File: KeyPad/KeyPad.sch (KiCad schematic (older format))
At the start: 9 parts, among them P1 CONN_01X03, SW1 SW_Push_Dual, SW2 SW_Push_Dual, SW3 SW_Push_Dual, SW4 SW_Push_Dual

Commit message: Pcb enrrutada y esquinas redondeadas
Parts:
- P1: footprint (none) -> Connectors_JST:JST_PH_S3B-PH-K_03x2.00mm_Angled
- R1, R2, R3, R4: footprint (none) -> Resistors_SMD:R_0805
- SW1, SW2, SW3, SW4: footprint (none) -> Buttons_Switches_THT:SW_PUSH-12mm
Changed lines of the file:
@@
 F 0 "SW1" H 5700 2800 50  0000 L CNN
 F 1 "SW_Push_Dual" H 5650 2430 50  0000 C CNN
-F 2 "" H 5650 2900 50  0001 C CNN
+F 2 "Buttons_Switches_THT:SW_PUSH-12mm" H 5650 2900 50  0001 C CNN
 F 3 "" H 5650 2900 50  0001 C CNN
 	1    5650 2700
@@
 F 0 "SW2" H 5700 3400 50  0000 L CNN
 F 1 "SW_Push_Dual" H 5650 3030 50  0000 C CNN
-F 2 "" H 5650 3500 50  0001 C CNN
+F 2 "Buttons_Switches_THT:SW_PUSH-12mm" H 5650 3500 50  0001 C CNN
 F 3 "" H 5650 3500 50  0001 C CNN
 	1    5650 3300
@@
 F 0 "SW3" H 5700 4050 50  0000 L CNN
 F 1 "SW_Push_Dual" H 5650 3680 50  0000 C CNN
-F 2 "" H 5650 4150 50  0001 C CNN
+F 2 "Buttons_Switches_THT:SW_PUSH-12mm" H 5650 4150 50  0001 C CNN
 F 3 "" H 5650 4150 50  0001 C CNN
 	1    5650 3950
@@
 F 0 "SW4" H 5700 4650 50  0000 L CNN
 F 1 "SW_Push_Dual" H 5650 4280 50  0000 C CNN
-F 2 "" H 5650 4750 50  0001 C CNN
+F 2 "Buttons_Switches_THT:SW_PUSH-12mm" H 5650 4750 50  0001 C CNN
 F 3 "" H 5650 4750 50  0001 C CNN
 	1    5650 4550
@@
 F 0 "R2" V 5280 3100 50  0000 C CNN
 F 1 "330R" V 5200 3100 50  0000 C CNN
-F 2 "" V 5130 3100 50  0001 C CNN
+F 2 "Resistors_SMD:R_0805" V 5130 3100 50  0001 C CNN
 F 3 "" H 5200 3100 50  0001 C CNN
 	1    5200 3100
@@
 F 0 "P1" H 4250 3100 50  0000 C CNN
 F 1 "CONN_01X03" V 4350 2900 50  0000 C CNN
-F 2 "" H 4250 2900 50  0001 C CNN
+F 2 "Connectors_JST:JST_PH_S3B-PH-K_03x2.00mm_Angled" H 4250 2900 50  0001 C CNN
 F 3 "" H 4250 2900 50  0001 C CNN
 	1    4250 2900
@@
 F 0 "R3" V 5280 3750 50  0000 C CNN
 F 1 "620R" V 5200 3750 50  0000 C CNN
-F 2 "" V 5130 3750 50  0001 C CNN
+F 2 "Resistors_SMD:R_0805" V 5130 3750 50  0001 C CNN
 F 3 "" H 5200 3750 50  0001 C CNN
 	1    5200 3750
@@
 F 0 "R4" V 5280 4350 50  0000 C CNN
 F 1 "1K" V 5200 4350 50  0000 C CNN
-F 2 "" V 5130 4350 50  0001 C CNN
+F 2 "Resistors_SMD:R_0805" V 5130 4350 50  0001 C CNN
 F 3 "" H 5200 4350 50  0001 C CNN
 	1    5200 4350
@@
 F 0 "R1" V 5280 2450 50  0000 C CNN
 F 1 "2K" V 5200 2450 50  0000 C CNN
-F 2 "" V 5130 2450 50  0001 C CNN
+F 2 "Resistors_SMD:R_0805" V 5130 2450 50  0001 C CNN
 F 3 "" H 5200 2450 50  0001 C CNN
 	1    5200 2450

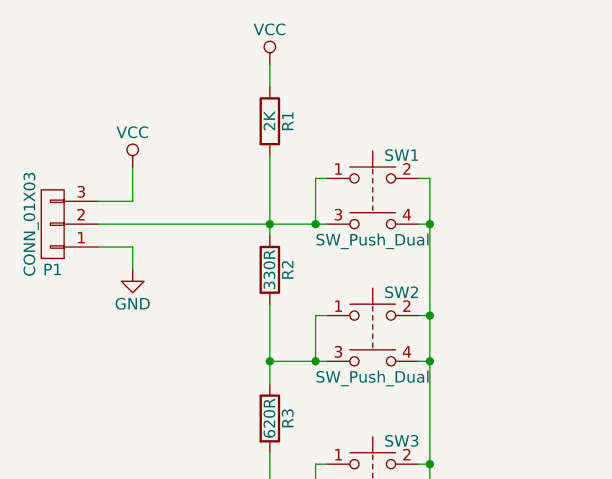
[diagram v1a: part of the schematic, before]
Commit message: Error del conector reparado
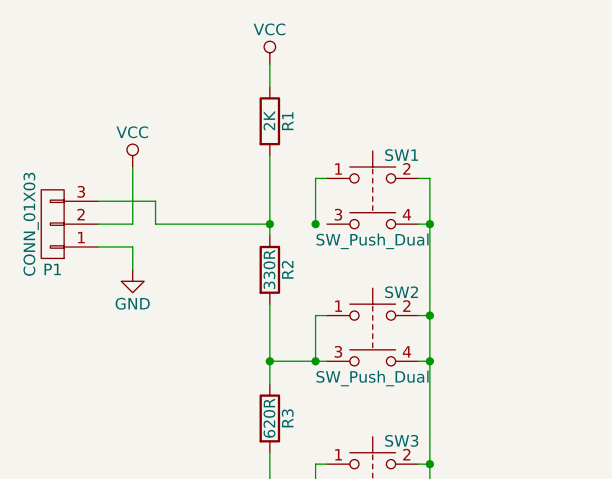
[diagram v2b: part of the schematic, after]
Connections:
- net VCC: now also P1.2 (P2); no longer P1.3 (P3)
- new net: P1.3 (P3), R1.2, R2.1
- now unconnected: SW1.1, SW1.3
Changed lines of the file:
@@
 	1    0    0    -1
 $EndComp
-Wire Wire Line
-	4450 2800 4600 2800
-Wire Wire Line
-	4600 2800 4600 2650
-Wire Wire Line
-	4450 2900 5450 2900
 $Comp
 L PWR_FLAG #FLG05
@@
 Wire Wire Line
 	6400 6850 6400 7150
+Wire Wire Line
+	5200 2900 4700 2900
+Wire Wire Line
+	4700 2900 4700 2800
+Wire Wire Line
+	4700 2800 4450 2800
+Wire Wire Line
+	4600 2650 4600 2900
+Wire Wire Line
+	4600 2900 4450 2900
 $EndSCHEMATC
